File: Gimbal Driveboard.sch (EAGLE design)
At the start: 26 parts, among them J2 APP_2POS_CONFIG12V_HORIZ, U1 OKI-78SR-5/1.5-W36HC, U2 MAX232D, U3 MAX232D

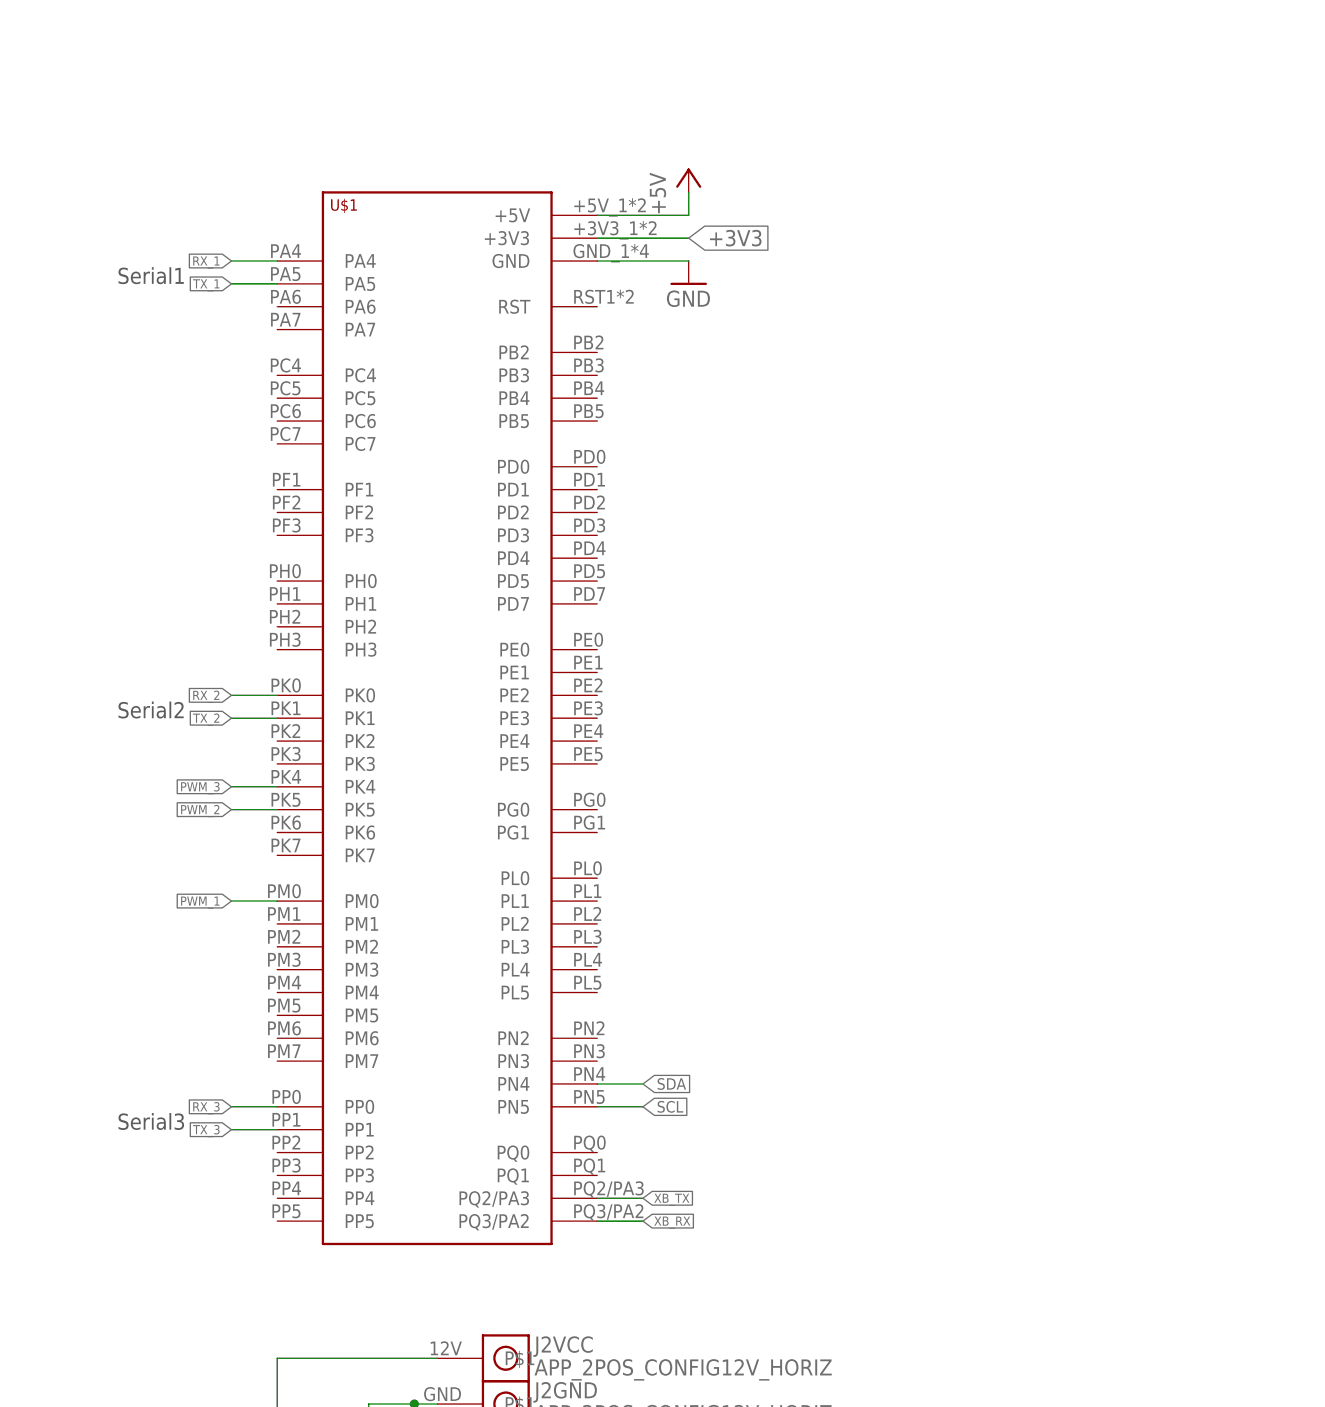
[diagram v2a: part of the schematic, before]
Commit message: removed TIVA holes on outside of board and rotated silkscreen
I replaced the TIVA package with just the ehaders and re-assigned all the pins in the schematic to match the physical layout on the old package. I rotated the silkscreen 180 so it is oriented right when it is mounted to rover.
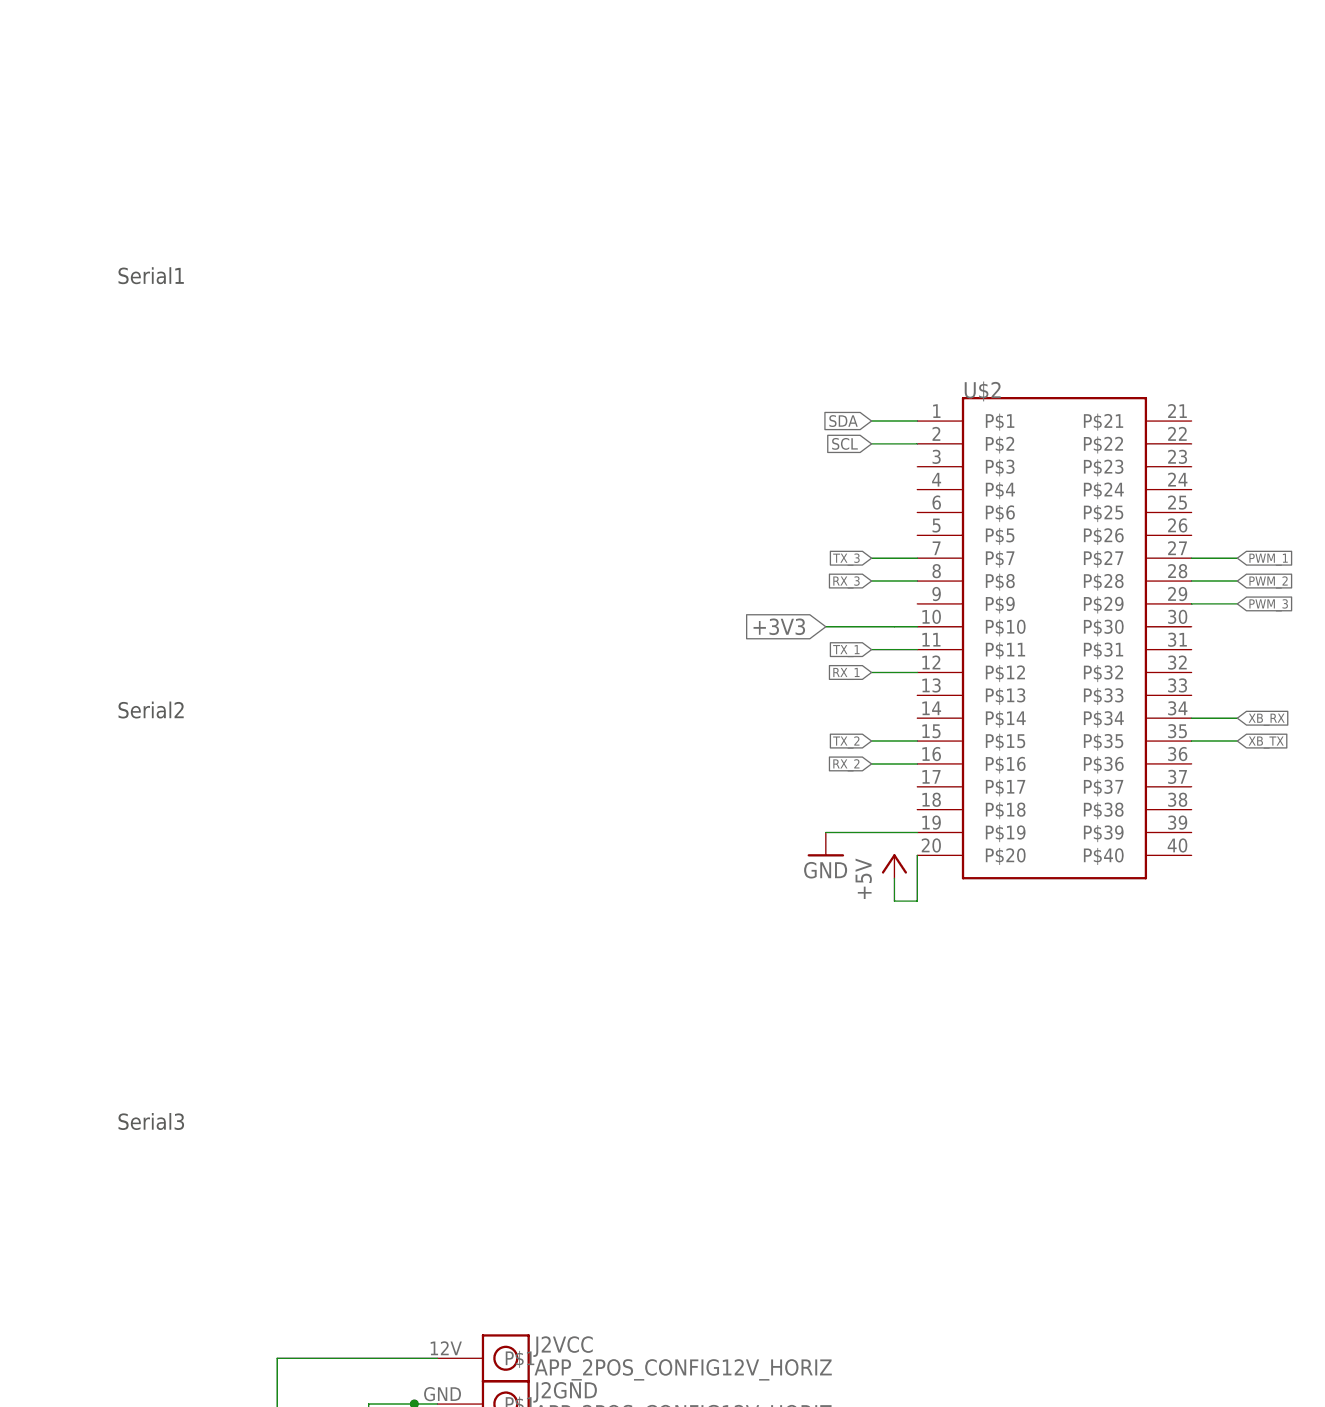
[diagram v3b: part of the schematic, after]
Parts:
- removed U$1: TIVA-1294, MRDT-Microcontrollers:TIVA-1294
- added U$2: TI_BACKPACK_HEADER, TI_HEADERS:TI_BACKPACK_HEADER
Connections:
- net +3V3: now also U$2.P$10; no longer U$1.+3V3
- net +5V: now also U$2.P$20; no longer U$1.+5V
- net GND: now also U$2.P$19; no longer U$1.GND
- net PWM_1: now also U$2.P$27; no longer U$1.PM0
- net PWM_2: now also U$2.P$28; no longer U$1.PK5
- net PWM_3: now also U$2.P$29; no longer U$1.PK4
- net RX_1: now also U$2.P$12; no longer U$1.PA4
- net RX_2: now also U$2.P$16; no longer U$1.PK0
- net RX_3: now also U$2.P$8; no longer U$1.PP0
- net SCL: now also U$2.P$2; no longer U$1.PN5
- net SDA: now also U$2.P$1; no longer U$1.PN4
- net TX_1: now also U$2.P$11; no longer U$1.PA5
- net TX_2: now also U$2.P$15; no longer U$1.PK1
- net TX_3: now also U$2.P$7; no longer U$1.PP1
- net XB_RX: now also U$2.P$34; no longer U$1.PQ3/PA2
- net XB_TX: now also U$2.P$35; no longer U$1.PQ2/PA3

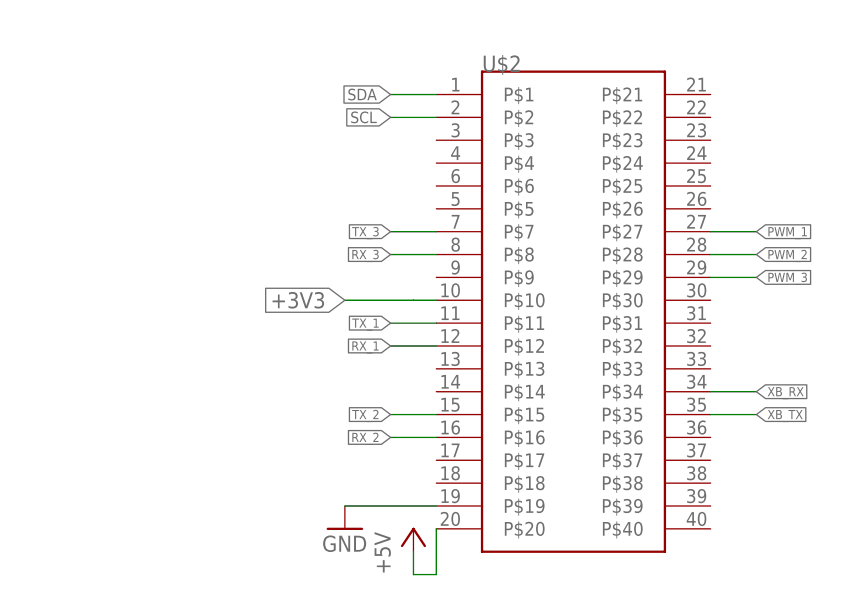
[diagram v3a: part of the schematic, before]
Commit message: Re-routed XB Serial to Serial 2
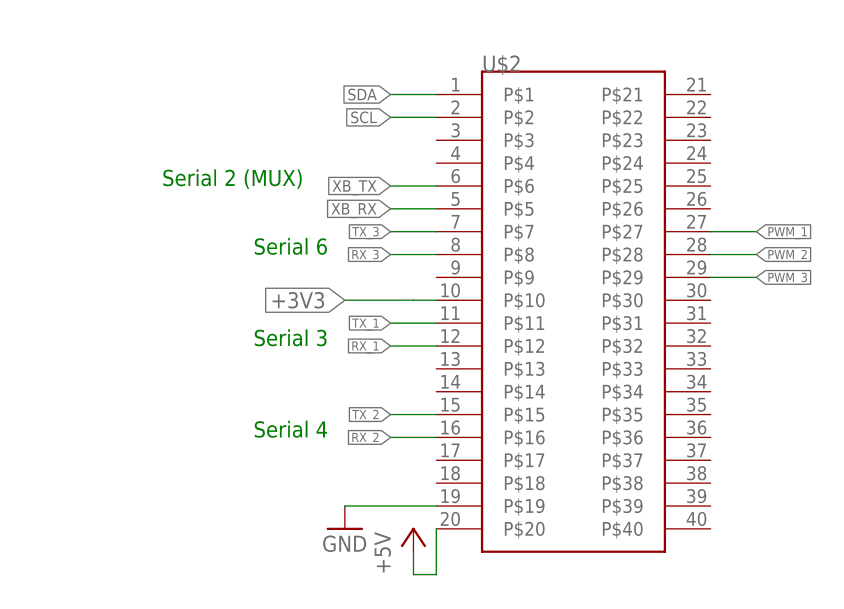
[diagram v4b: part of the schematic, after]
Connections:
- net XB_RX: now also U$2.P$5; no longer U$2.P$34
- net XB_TX: now also U$2.P$6; no longer U$2.P$35
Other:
- note added: "Serial 2 (MUX)"
- note added: "Serial 3"
- note added: "Serial 4"
- note added: "Serial 6"
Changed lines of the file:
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@@
 <text x="152.4" y="30.48" size="2.54" layer="97">Serial2</text>
 <text x="152.4" y="2.54" size="2.54" layer="97">Serial3</text>
+<text x="248.92" y="58.42" size="1.778" layer="91">Serial 6</text>
+<text x="248.92" y="48.26" size="1.778" layer="91">Serial 3</text>
+<text x="248.92" y="38.1" size="1.778" layer="91">Serial 4</text>
+<text x="238.76" y="66.04" size="1.778" layer="91">Serial 2 (MUX)</text>
 </plain>
 <instances>
@@
 </segment>
 <segment>
-<label x="304.8" y="43.18" size="1.016" layer="95" xref="yes"/>
-<pinref part="U$2" gate="G$1" pin="P$34"/>
-<wire x1="304.8" y1="43.18" x2="299.72" y2="43.18" width="0.1524" layer="91"/>
+<pinref part="U$2" gate="G$1" pin="P$5"/>
+<wire x1="269.24" y1="63.5" x2="264.16" y2="63.5" width="0.1524" layer="91"/>
+<label x="264.16" y="63.5" size="1.27" layer="95" rot="R180" xref="yes"/>
 </segment>
 </net>
@@
 </segment>
 <segment>
-<label x="304.8" y="40.64" size="1.016" layer="95" xref="yes"/>
-<pinref part="U$2" gate="G$1" pin="P$35"/>
-<wire x1="304.8" y1="40.64" x2="299.72" y2="40.64" width="0.1524" layer="91"/>
-</segment>
-</net>
+<pinref part="U$2" gate="G$1" pin="P$6"/>
+<wire x1="269.24" y1="66.04" x2="264.16" y2="66.04" width="0.1524" layer="91"/>
+<label x="264.16" y="66.04" size="1.27" layer="95" rot="R180" xref="yes"/>
+</segment>
+</net>
